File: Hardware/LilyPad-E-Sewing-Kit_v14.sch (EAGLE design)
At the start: 51 parts

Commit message: Updated files
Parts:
- removed LED+2, LED+3, LED+4, LED-2, LED-3, LED-4: SEWTAP6, LilyPad-Wearables:SEWTAP6
- removed LED2, LED3, LED4: White, SparkFun-3-2-07:LED1206
- removed R10, R11, R9: 100, SparkFun:RESISTOR0603-RES
- removed U$10, U$11, U$12, U$15, U$16, U$17: MOUSE-BITE-12_HOLES, Testing:MOUSE-BITE-12_HOLES
- added FRAME1: FRAME-LETTER, SparkFun-Aesthetics:FRAME-LETTER
- added S1: (no value), SparkFun-Electromechanical:SWITCH-SPDTSMD
- added U$5: REVISION, SparkFun-Aesthetics:REVISION
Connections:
- removed net N$24: LED2.C, R9.1
- removed net N$27: LED3.C, R10.1
- removed net N$30: LED4.C, R11.1
- new net N$1: BAT1.-, S1.P
- net GND: no longer BAT1.-, LED-2.1, LED-3.1, LED-4.1, R10.2, R11.2, R9.2, U$15.P$1, U$16.P$1, U$17.P$1
- net SWITCH: no longer LED+2.1, LED+3.1, LED+4.1, LED2.A, LED3.A, LED4.A, U$10.P$1, U$11.P$1, U$12.P$1
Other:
- note added: "Changes to V14"
- note added: "Mary West"
- note added: "Removed two LEDs. added Switched Coin Cell battery holder"
- note added: "v14"
- note removed: "Changes to V13"
- note removed: "Rotated Lilypad silk Added OSHW and SFE flame"
- note removed: "v13"
- moved on the sheet: BAT1

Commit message: Updated board and schemtic files
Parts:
- removed JP2: LOGO-SFESK, SparkFun-Aesthetics:LOGO-SFESK
- added LED+2, LED-2: SEWTAP6, LilyPad-Wearables:SEWTAP6
- added LED2: White, SparkFun-3-2-07:LED1206
- added LOGO1: SFE_LOGO_FLAME.1_STOP, SparkFun-Aesthetics:SFE_LOGO_FLAME.1_STOP
- added R1: 180, SparkFun-Resistors:180OHM1/10W1%(0603)
- added U$10, U$9: MOUSE-BITE-12_HOLES, Testing:MOUSE-BITE-12_HOLES
- BAT1: value (none) -> 20mm coincell; device Testing:BATTERYBATTCON_20MM_4LEGS -> SparkFun-Electromechanical:BATTERY20MM_4LEGS
- JP1, JP4: value FIDUCIAL1X2 -> FIDUCIALUFIDUCIAL; device SparkFun:FIDUCIAL1X2 -> SparkFun-Aesthetics:FIDUCIALUFIDUCIAL
- R, R8: value 100 -> 180; device SparkFun:RESISTOR0603-RES -> SparkFun-Resistors:180OHM1/10W1%(0603)
- S2: value AYZ0202 -> DPDT; device SparkFun:AYZ0202 -> SparkFun-Electromechanical:SWITCH-DPDTAYZ0202
- S3: value (none) -> TAC_SWITCHSMD; device SparkFun:TAC_SWITCHSMD -> SparkFun-Retired:TAC_SWITCHSMD
- renumbered U$1 to ST1, U$2 to ST2, U$3 to ST3, U$4 to ST4
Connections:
- new net GND1: LED-2.1, R1.2
- new net N$2: LED2.C, R1.1
- new net SWITCH1: LED+2.1, LED2.A
- net GND: now also S1.O, U$10.P$1
- net SWITCH: now also U$9.P$1
- net VCC: no longer U$6.P$1

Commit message: Added PROD-IDs
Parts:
- LED, LED1, LED2: value White -> WHITE; device SparkFun-3-2-07:LED1206 -> SparkFun-LED:LED-WHITE1206
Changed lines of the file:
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@@
 <layer number="113" name="IDFDebug" color="4" fill="1" visible="yes" active="yes"/>
 <layer number="116" name="Patch_BOT" color="9" fill="4" visible="yes" active="yes"/>
+<layer number="118" name="Rect_Pads" color="7" fill="1" visible="yes" active="yes"/>
 <layer number="121" name="_tsilk" color="7" fill="1" visible="yes" active="yes"/>
 <layer number="122" name="_bsilk" color="7" fill="1" visible="yes" active="yes"/>
@@
 <part name="LED+" library="LilyPad-Wearables" deviceset="SEWTAP" device="6"/>
 <part name="LED-" library="LilyPad-Wearables" deviceset="SEWTAP" device="6"/>
-<part name="LED" library="SparkFun-3-2-07" deviceset="LED" device="1206" value="White"/>
+<part name="LED" library="SparkFun-LED" deviceset="LED-WHITE" device="1206" value="WHITE"/>
 <part name="R8" library="SparkFun-Resistors" deviceset="180OHM1/10W1%(0603)" device="" value="180"/>
 <part name="LED+1" library="LilyPad-Wearables" deviceset="SEWTAP" device="6"/>
 <part name="LED-1" library="LilyPad-Wearables" deviceset="SEWTAP" device="6"/>
-<part name="LED1" library="SparkFun-3-2-07" deviceset="LED" device="1206" value="White"/>
+<part name="LED1" library="SparkFun-LED" deviceset="LED-WHITE" device="1206" value="WHITE"/>
 <part name="U$13" library="Testing" deviceset="MOUSE-BITE-1" device="2_HOLES"/>
 <part name="U$14" library="Testing" deviceset="MOUSE-BITE-1" device="2_HOLES"/>
@@
 <part name="LED+2" library="LilyPad-Wearables" deviceset="SEWTAP" device="6"/>
 <part name="LED-2" library="LilyPad-Wearables" deviceset="SEWTAP" device="6"/>
-<part name="LED2" library="SparkFun-3-2-07" deviceset="LED" device="1206" value="White"/>
+<part name="LED2" library="SparkFun-LED" deviceset="LED-WHITE" device="1206" value="WHITE"/>
 <part name="U$9" library="Testing" deviceset="MOUSE-BITE-1" device="2_HOLES"/>
 <part name="U$10" library="Testing" deviceset="MOUSE-BITE-1" device="2_HOLES"/>
@@
 <wire x1="68.58" y1="109.22" x2="68.58" y2="106.68" width="0.1524" layer="91"/>
 <junction x="68.58" y="106.68"/>
-<label x="63.5" y="106.68" size="1.778" layer="95"/>
 <pinref part="BAT1" gate="G$1" pin="+"/>
 <pinref part="ST2" gate="G$1" pin="1"/>

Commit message: Updated Resistor Value
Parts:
- R, R1, R8: value 180 -> 150; device SparkFun-Resistors:180OHM1/10W1%(0603) -> SparkFun-Resistors:150OHM-1/10W-1%(0603)
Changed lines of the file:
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@@
 <part name="BUTTONS" library="LilyPad-Wearables" deviceset="SEWTAP" device="4" value="SEWTAP8"/>
 <part name="BUTTON-" library="LilyPad-Wearables" deviceset="SEWTAP" device="4" value="SEWTAP8"/>
-<part name="R" library="SparkFun-Resistors" deviceset="180OHM1/10W1%(0603)" device="" value="180"/>
+<part name="R" library="SparkFun-Resistors" deviceset="150OHM-1/10W-1%(0603)" device="" value="150"/>
 <part name="LED+" library="LilyPad-Wearables" deviceset="SEWTAP" device="6"/>
 <part name="LED-" library="LilyPad-Wearables" deviceset="SEWTAP" device="6"/>
 <part name="LED" library="SparkFun-LED" deviceset="LED-WHITE" device="1206" value="WHITE"/>
-<part name="R8" library="SparkFun-Resistors" deviceset="180OHM1/10W1%(0603)" device="" value="180"/>
+<part name="R8" library="SparkFun-Resistors" deviceset="150OHM-1/10W-1%(0603)" device="" value="150"/>
 <part name="LED+1" library="LilyPad-Wearables" deviceset="SEWTAP" device="6"/>
 <part name="LED-1" library="LilyPad-Wearables" deviceset="SEWTAP" device="6"/>
@@
 <part name="S1" library="SparkFun-Electromechanical" deviceset="SWITCH-SPDT" device="SMD"/>
 <part name="U$5" library="SparkFun-Aesthetics" deviceset="REVISION" device=""/>
-<part name="R1" library="SparkFun-Resistors" deviceset="180OHM1/10W1%(0603)" device="" value="180"/>
+<part name="R1" library="SparkFun-Resistors" deviceset="150OHM-1/10W-1%(0603)" device="" value="150"/>
 <part name="LED+2" library="LilyPad-Wearables" deviceset="SEWTAP" device="6"/>
 <part name="LED-2" library="LilyPad-Wearables" deviceset="SEWTAP" device="6"/>

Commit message: Updated files
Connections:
- net VCC: now also U$6.P$1
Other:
- moved on the sheet: BAT1, BUTTON-, BUTTONS, LED, LED+, LED+1, LED+2, LED-, LED-1, LED-2, LED1, LED2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

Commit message: Updated Brd and Sch files (in Sync)
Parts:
- removed JP1, JP4: FIDUCIALUFIDUCIAL, SparkFun-Aesthetics:FIDUCIALUFIDUCIAL
- removed LED: WHITE, SparkFun-LED:LED-WHITE1206
- removed LED+, LED-, ST1, ST3: SEWTAP6, LilyPad-Wearables:SEWTAP6
- removed LOGO1: SFE_LOGO_FLAME.1_STOP, SparkFun-Aesthetics:SFE_LOGO_FLAME.1_STOP
- removed R, R8: 150, SparkFun-Resistors:150OHM-1/10W-1%(0603)
- removed U$5: REVISION, SparkFun-Aesthetics:REVISION
- removed U$8: OSHW-LOGOS, SparkFun-Aesthetics:OSHW-LOGOS
- added BATB-, BATB-2, LED+3, LED-3: SEWTAP6, LilyPad-Wearables:SEWTAP6
- added LED3: WHITE, SparkFun-LED:LED-WHITE1206
- added R2, R3: 150, SparkFun-Resistors:150OHM-1/10W-1%(0603)
- added U$1: REVISION, SparkFun-Aesthetics:REVISION
- BUTTON-, BUTTONS, SLIDEOFF, SLIDEON: device LilyPad-Wearables:SEWTAP4 -> LilyPad-Wearables:SEWTAP8
- S2: value DPDT -> SWITCH-MOMENTARY-2SMD; device SparkFun-Electromechanical:SWITCH-DPDTAYZ0202 -> SparkFun-Electromechanical:SWITCH-MOMENTARY-2SMD
- S3: value TAC_SWITCHSMD -> (none); device SparkFun-Retired:TAC_SWITCHSMD -> SparkFun-Electromechanical:SWITCH-SPDTSMD
- renumbered ST2 to BATT+2, ST4 to BATT+, U$10 to MB6, U$13 to MB3, U$14 to MB4, U$18 to MB8, U$19 to MB7, U$40 to MB2, U$42 to MB9, U$44 to MB10, U$46 to MB1, U$6 to MB+, U$7 to MB-, U$9 to MB5
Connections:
- removed net GND1: LED-2.1, R1.2
- removed net N$18: LED.C, R.1
- removed net N$21: LED1.C, R8.1
- removed net SINK1: S2.6
- removed net SINK2: S2.3
- removed net SWITCH1: LED+2.1, LED2.A
- removed net VCC: BAT1.+, BATT+.1, BATT+2.1, BUTTON-.1, MB+.P$1, MB1.P$1, MB2.P$1, S2.1, S2.4, S3.4, SLIDEON.1
- new net N$11: LED1.C, R1.1
- new net N$12: LED2.C, R2.1
- new net N$13: LED3.C, R3.1
- net BUTTON: now also S2.1; no longer S3.2
- net GND: now also BAT1.-, BATB-.1, BATB-2.1, LED-2.1, LED-3.1, R1.2, R2.2, R3.2; no longer LED-.1, R.2, R8.2, S1.O, ST1.1, ST3.1
- net N$1: now also BAT1.+; no longer BAT1.-
- net N$2: now also BATT+.1, BATT+2.1, BUTTON-.1, MB+.P$1, MB1.P$1, S1.O, S2.2, S3.O, SLIDEON.1; no longer LED2.C, R1.1
- net SWITCH: now also LED+2.1, LED+3.1, LED2.A, LED3.A, S3.P; no longer LED+.1, LED.A, S2.2, S2.5
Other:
- note added: "L. Buechley, N. Seidle, P. Lewis, T. Klopfenstein"
- note added: "M. West"
- note added: "Removed two LEDs, added Switched Coin Cell battery holder"
- note removed: "L. Buechley, N.Seidle, P. Lewis T. Klopfenstein"
- note removed: "Mary West"
- note removed: "Removed two LEDs. added Switched Coin Cell battery holder"
- moved on the sheet: BAT1, LED+2, LED-1, LED-2, LED2, R1, S1, SLIDEOFF, SLIDEON

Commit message: Chnages per QC checklist
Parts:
- added FD1, FD2: FIDUCIALUFIDUCIAL, SparkFun-Aesthetics:FIDUCIALUFIDUCIAL
- added LOGO1: SFE_LOGO_FLAME.1COP, SparkFun-Aesthetics:SFE_LOGO_FLAME.1COP
- added LOGO2: OSHW-LOGOS, SparkFun-Aesthetics:OSHW-LOGOS
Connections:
- net N$2: now also MB2.P$1
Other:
- moved on the sheet: BAT1, BATB-, BATB-2, BATT+, BATT+2, BUTTON-, BUTTONS, LED+1, LED+2, LED+3, LED-1, LED-2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

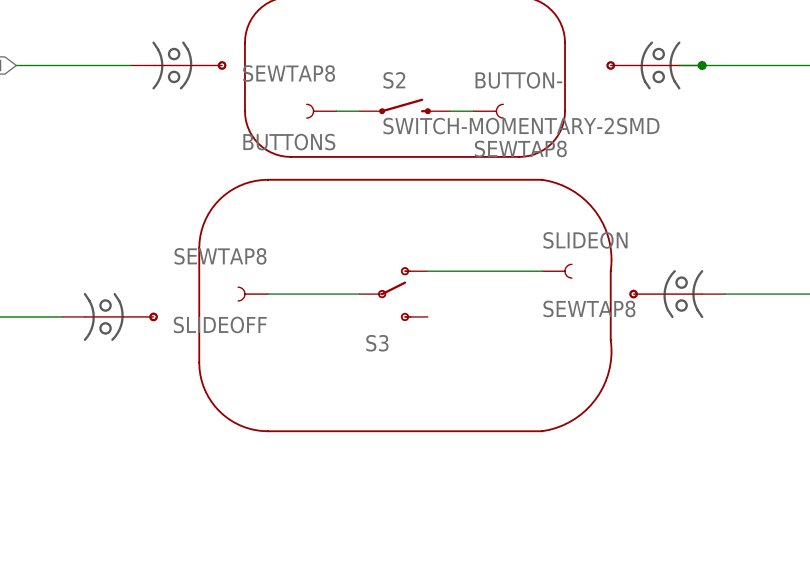
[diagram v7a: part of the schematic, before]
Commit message: Approved DRC Erros
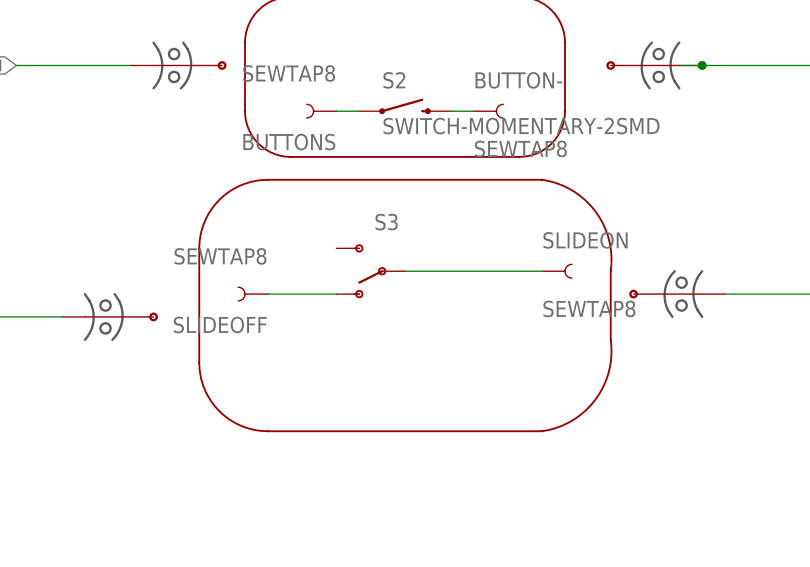
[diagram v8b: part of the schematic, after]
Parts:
- LOGO1: value SFE_LOGO_FLAME.1COP -> SFE_LOGO_FLAME.1_INCH; device SparkFun-Aesthetics:SFE_LOGO_FLAME.1COP -> SparkFun-Aesthetics:SFE_LOGO_FLAME.1_INCH
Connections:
- new net N$3: S3.O, SLIDEOFF.1
- net N$2: now also S3.P; no longer S3.O
- net SWITCH: no longer S3.P, SLIDEOFF.1
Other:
- moved on the sheet: S3
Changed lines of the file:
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@@
 <part name="FRAME1" library="SparkFun-Aesthetics" deviceset="FRAME-LETTER" device=""/>
 <part name="U$1" library="SparkFun-Aesthetics" deviceset="REVISION" device=""/>
-<part name="LOGO1" library="SparkFun-Aesthetics" deviceset="SFE_LOGO_FLAME" device=".1COP"/>
+<part name="LOGO1" library="SparkFun-Aesthetics" deviceset="SFE_LOGO_FLAME" device=".1_INCH" value="SFE_LOGO_FLAME.1_INCH"/>
 <part name="LOGO2" library="SparkFun-Aesthetics" deviceset="OSHW-LOGO" device="S" value="OSHW-LOGOS"/>
 <part name="FD1" library="SparkFun-Aesthetics" deviceset="FIDUCIAL" device="UFIDUCIAL"/>
@@
 <instance part="S1" gate="1" x="43.18" y="137.16"/>
 <instance part="S2" gate="G$1" x="170.18" y="124.46"/>
-<instance part="S3" gate="1" x="167.64" y="104.14"/>
+<instance part="S3" gate="1" x="167.64" y="106.68" rot="R180"/>
 <instance part="FRAME1" gate="G$1" x="0" y="0"/>
 <instance part="FRAME1" gate="V" x="147.32" y="0"/>
@@
 </segment>
 <segment>
-<pinref part="S3" gate="1" pin="O"/>
 <pinref part="SLIDEON" gate="G$1" pin="1"/>
-<wire x1="172.72" y1="106.68" x2="185.42" y2="106.68" width="0.1524" layer="91"/>
+<wire x1="185.42" y1="106.68" x2="170.18" y2="106.68" width="0.1524" layer="91"/>
+<pinref part="S3" gate="1" pin="P"/>
 </segment>
 </net>
@@
 <wire x1="60.96" y1="55.88" x2="60.96" y2="53.34" width="0.1524" layer="91"/>
 </segment>
-<segment>
-<pinref part="S3" gate="1" pin="P"/>
-<pinref part="SLIDEOFF" gate="G$1" pin="1"/>
-<wire x1="165.1" y1="104.14" x2="154.94" y2="104.14" width="0.1524" layer="91"/>
-</segment>
 </net>
 <net name="N$11" class="0">
@@
 </segment>
 </net>
+<net name="N$3" class="0">
+<segment>
+<pinref part="S3" gate="1" pin="O"/>
+<pinref part="SLIDEOFF" gate="G$1" pin="1"/>
+<wire x1="162.56" y1="104.14" x2="154.94" y2="104.14" width="0.1524" layer="91"/>
+</segment>
+</net>
